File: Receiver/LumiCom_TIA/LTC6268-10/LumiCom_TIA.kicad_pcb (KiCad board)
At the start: 4 copper layers, 90 x 40 mm, 52 parts, among them J1 TEST, J10 OUT, J2 Conn_Coaxial, J3 Vout, J4 N_EN, J5 N_ALC, J6 Conn_Coaxial, J7 IN, J8 Vout, J9 TEST, U1 XLMH34400IDRLR, U2 LTC6268-10-SOT23

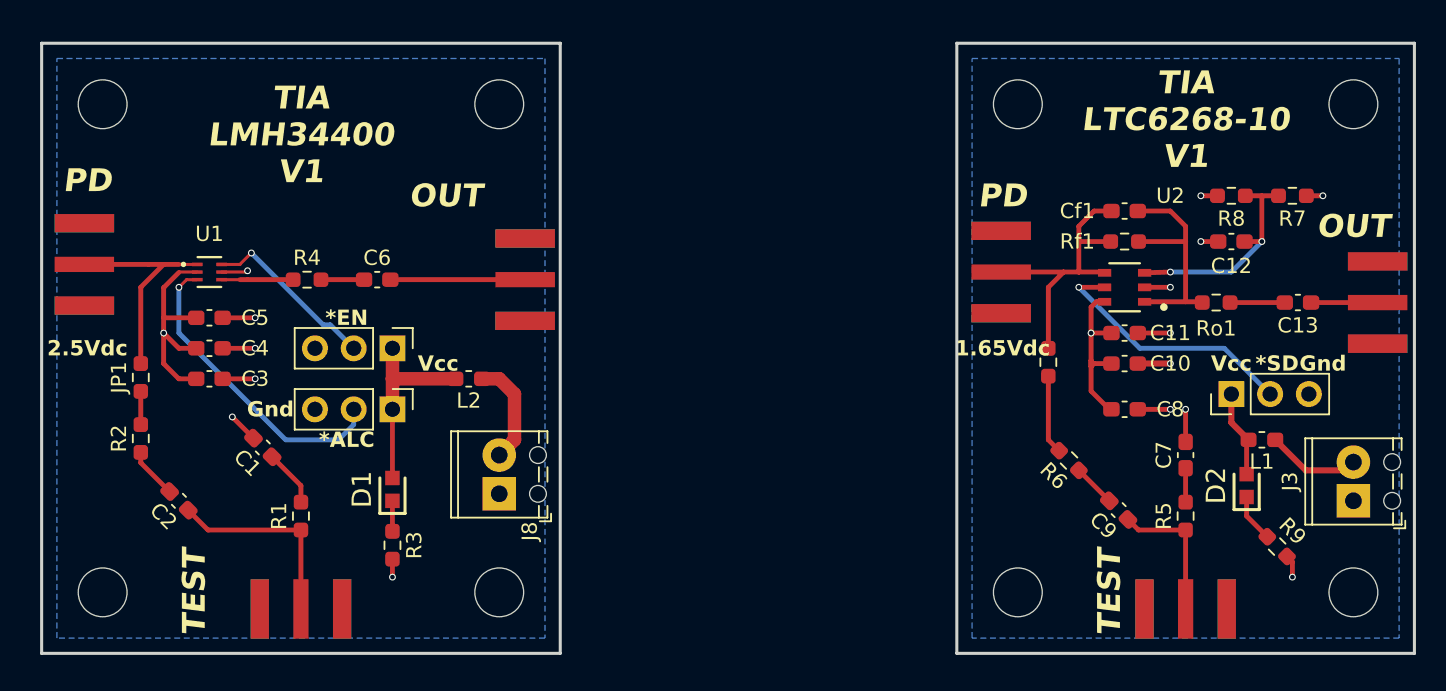
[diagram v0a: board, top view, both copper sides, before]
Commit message: Multiple updates
SMA, Screw terminals, track widths, added some optional 0 ohm bypass resistors
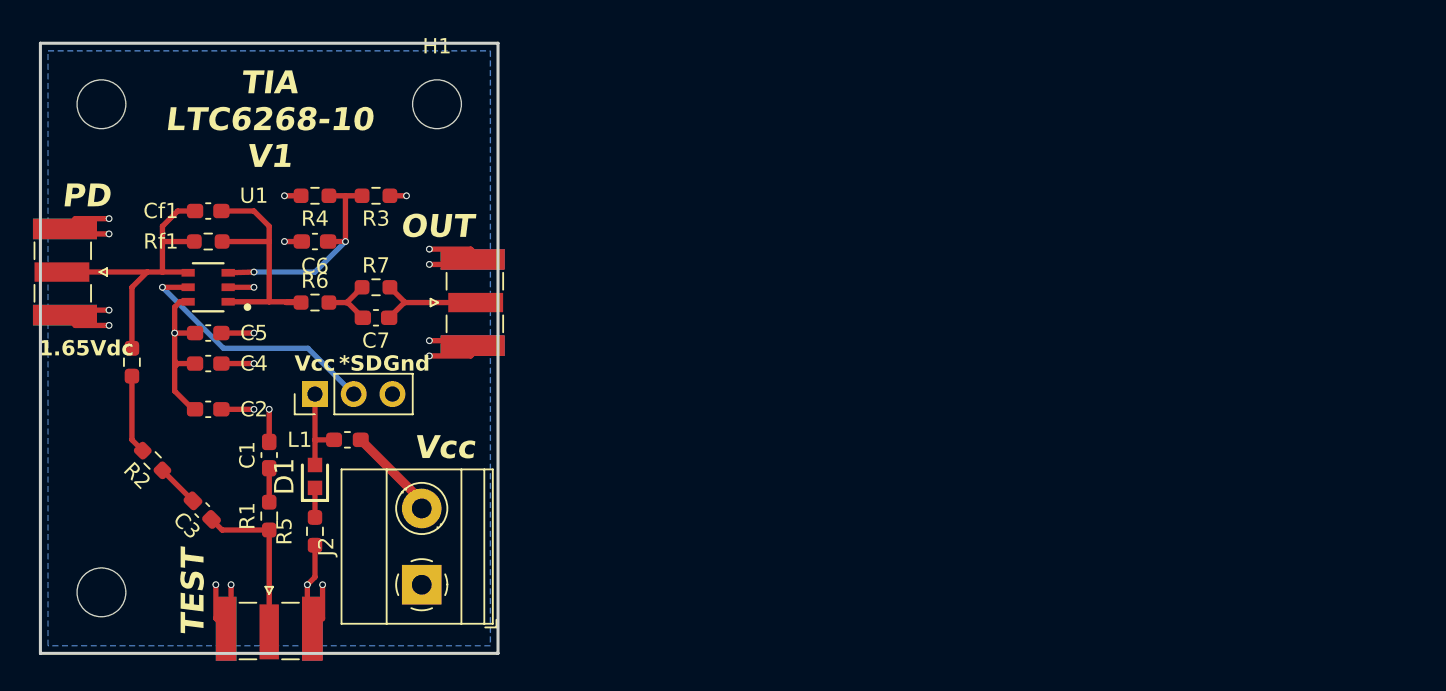
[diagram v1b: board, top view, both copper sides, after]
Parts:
- removed the C1 at (121.5, 79.5)
- removed the C2 at (116.0, 83.0)
- removed the C3 at (118.0, 75.0)
- removed the C4 at (118.0, 73.0)
- removed the C5 at (118.0, 71.0)
- removed the C6 at (129.0, 68.5)
- removed the D1 at (130.0, 82.2)
- removed the H2 at (137.0, 57.0)
- removed the H3 at (111.0, 89.0)
- removed H4, H5, H8: M3, MountingHole:MountingHole_3.2mm_M3_DIN965
- removed the J1 at (124.0, 91.4)
- removed the J2 at (108.5, 67.5)
- removed the J3 at (193.0, 83.0)
- removed the J4 at (130.0, 77.0)
- removed J5: N_ALC, Connector_PinHeader_2.54mm:PinHeader_1x03_P2.54mm_Vertical
- removed J6: Conn_Coaxial, LumiCom_TIA:RFSOLUTIONS_CON-SMA-EDGE-S
- removed the JP1 at (113.5, 74.9)
- removed L2: BLM18BA100SN1D, Inductor_SMD:L_0603_1608Metric_Pad1.05x0.95mm_HandSolder
- removed the R1 at (124.0, 84.0)
- removed the R2 at (113.5, 78.9)
- removed the R3 at (130.0, 85.9)
- removed the R4 at (124.4, 68.5)
- removed Ro1: 50, Resistor_SMD:R_0603_1608Metric_Pad0.98x0.95mm_HandSolder
- removed the U1 at (118.0, 68.0)
- added R6: 50, Resistor_SMD:R_0603_1608Metric_Pad0.98x0.95mm_HandSolder, F.Cu at (124.9, 70.0)
- added R7: 0, Resistor_SMD:R_0603_1608Metric_Pad0.98x0.95mm_HandSolder, F.Cu at (128.9, 69.0)
- J1: renamed from J7; footprint LumiCom_TIA:RFSOLUTIONS_CON-SMA-EDGE-S -> Connector_Coaxial:SMA_Samtec_SMA-J-P-X-ST-EM1_EdgeMount
- J2: renamed from J8; footprint TerminalBlock_Phoenix:TerminalBlock_Phoenix_MPT-0,5-2-2.54_1x02_P2.54mm_Horizontal -> TerminalBlock_Phoenix:TerminalBlock_Phoenix_MKDS-1,5-2_1x02_P5.00mm_Horizontal
- J3: renamed from J9; footprint LumiCom_TIA:RFSOLUTIONS_CON-SMA-EDGE-S -> Connector_Coaxial:SMA_Samtec_SMA-J-P-X-ST-EM1_EdgeMount
- J4: renamed from J10; footprint LumiCom_TIA:RFSOLUTIONS_CON-SMA-EDGE-S -> Connector_Coaxial:SMA_Samtec_SMA-J-P-X-ST-EM1_EdgeMount
- moved R5 63.1 mm to (124.9, 85.0), turned to -90 degrees
- moved D1 61.1 mm to (124.9, 81.4)
- moved J4 60.6 mm to (135.3, 70.0), turned to 90 degrees
- moved C7 60.5 mm to (128.9, 71.0)
- moved J1 60.1 mm to (108.5, 68.0), turned to -90 degrees
- moved C1 60.1 mm to (121.9, 80.0)
- moved C2 60.1 mm to (117.9, 77.0)
- moved C3 60.1 mm to (117.5, 83.6)
- moved C4 60.1 mm to (117.9, 74.0)
- moved C5 60.1 mm to (117.9, 72.0)
- moved C6 60.1 mm to (124.9, 66.0)
- moved Cf1 60.1 mm to (117.9, 64.0)
- moved H2 60.1 mm to (110.9, 89.0)
- moved H3 60.1 mm to (110.9, 57.0)
- moved J3 60.1 mm to (121.9, 91.4), turned to 0 degrees
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- renumbered C7 to C1, C8 to C2, C9 to C3, C10 to C4, C11 to C5, C12 to C6, C13 to C7, D2 to D1, H6 to H2, H7 to H3, JP2 to JP1, R5 to R1, R6 to R2, R7 to R3, R8 to R4, R9 to R5, U2 to U1
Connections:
- net /ltc6269-10/Shutdown_L renamed /Shutdown_L
- J2 pad 2: Net-(J8-Pin_2) -> Net-(J2-Pin_2)
- L1 pad 1: Net-(J3-Pin_2) -> Net-(J2-Pin_2)
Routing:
- net GND: track 25.2 -> 54.4 mm, vias 14 -> 19
- net VCC: track 45.8 -> 18.5 mm, vias 3 -> 2
- net Net-(J4-Pin_2): track 20.2 -> 0.00 mm, vias 1 -> 0
- net Net-(J2-In): track 14.5 -> 0.00 mm
- net Net-(J1-In) (its old number): track 13.1 -> 0.00 mm
- net Net-(J5-Pin_2): track 11.6 -> 0.00 mm, vias 1 -> 0
- net Net-(J6-In): track 9.73 -> 0.00 mm
- net Net-(J8-Pin_2): track 6.95 -> 0.00 mm
- net Net-(J3-Pin_2): track 6.18 -> 0.00 mm
- net Net-(J2-Pin_2): track 0.00 -> 6.16 mm
- net Net-(U1-OUT) (its old number): track 4.69 -> 0.00 mm
- net Net-(C1-Pad1) (its old number): track 3.76 -> 0.00 mm
- net Net-(C2-Pad2): track 3.35 -> 0.00 mm
- net Net-(C6-Pad1): track 2.82 -> 0.00 mm
- net Net-(J4-In): track 4.37 -> 6.56 mm
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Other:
- board size 90 x 40 mm -> 30 x 40 mm
- board text added: "Board thickness: 1.2mm 4 Layers"
- board text removed: "*ALC"
- board text removed: "*EN"
- board text removed: "2.5Vdc"
- board text removed: "TIA LMH34400 V1"
